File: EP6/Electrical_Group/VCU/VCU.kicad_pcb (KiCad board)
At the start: 4 copper layers, 150 x 120 mm, 328 parts, among them IC1 LMR50410Y3FQDBVRQ1, J1 MSD-4-A, J10 3V3out, J11 UPS_cap, J12 USBC_RPI_5Vonly, J13 USBA_RPI_5Vonly, J14 Rpi, J15 Dashboard, J16 STDC14, J17 CAN2, J18 CAN2_termination, J19 buzzer, J2 Conn_01x06, J20 I2C, J21 brakelight, J24 USB_C_stm32, J25 connector board, J3 I2C2, J4 NRST, J5 USART6, J6 DEBUG, J7 LVBattery, J8 24V_raw, J9 5Vout, Q1 AO3400A, Q2 2N7002, Q3 2N7002, SW1 VBUS, SW2 VBUS, U1 USB3300-EZK, U11 TCAN1042VDRQ1, U12 LSM6DSOX, U14 LM66100DCK, U15 USBLC6-2SC6, U2 STM32H743ZITx, U4 TPS5430DDA, U5 TPS5430DDA, U6 INA180A3, U7 INA180A3, U8 AMS1117-3.3, U9 LM66100DCK, Y1 8MHz X49SM8MSD2SC, Y2 32.768kHz Q13FC13500004, Y3 X322524MSB4SI

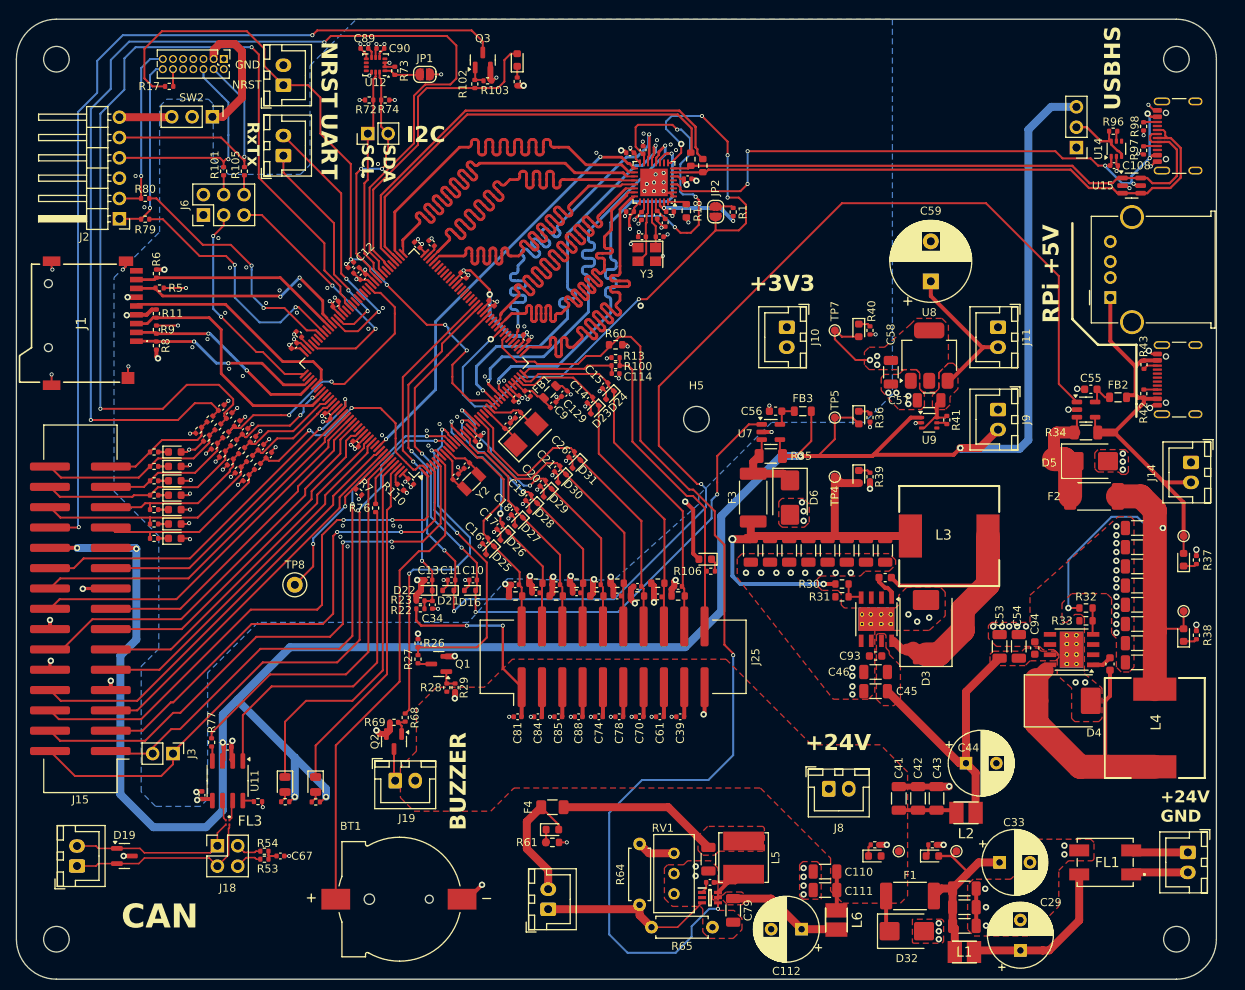
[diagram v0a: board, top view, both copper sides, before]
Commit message: add silkscreen on VCU PCB
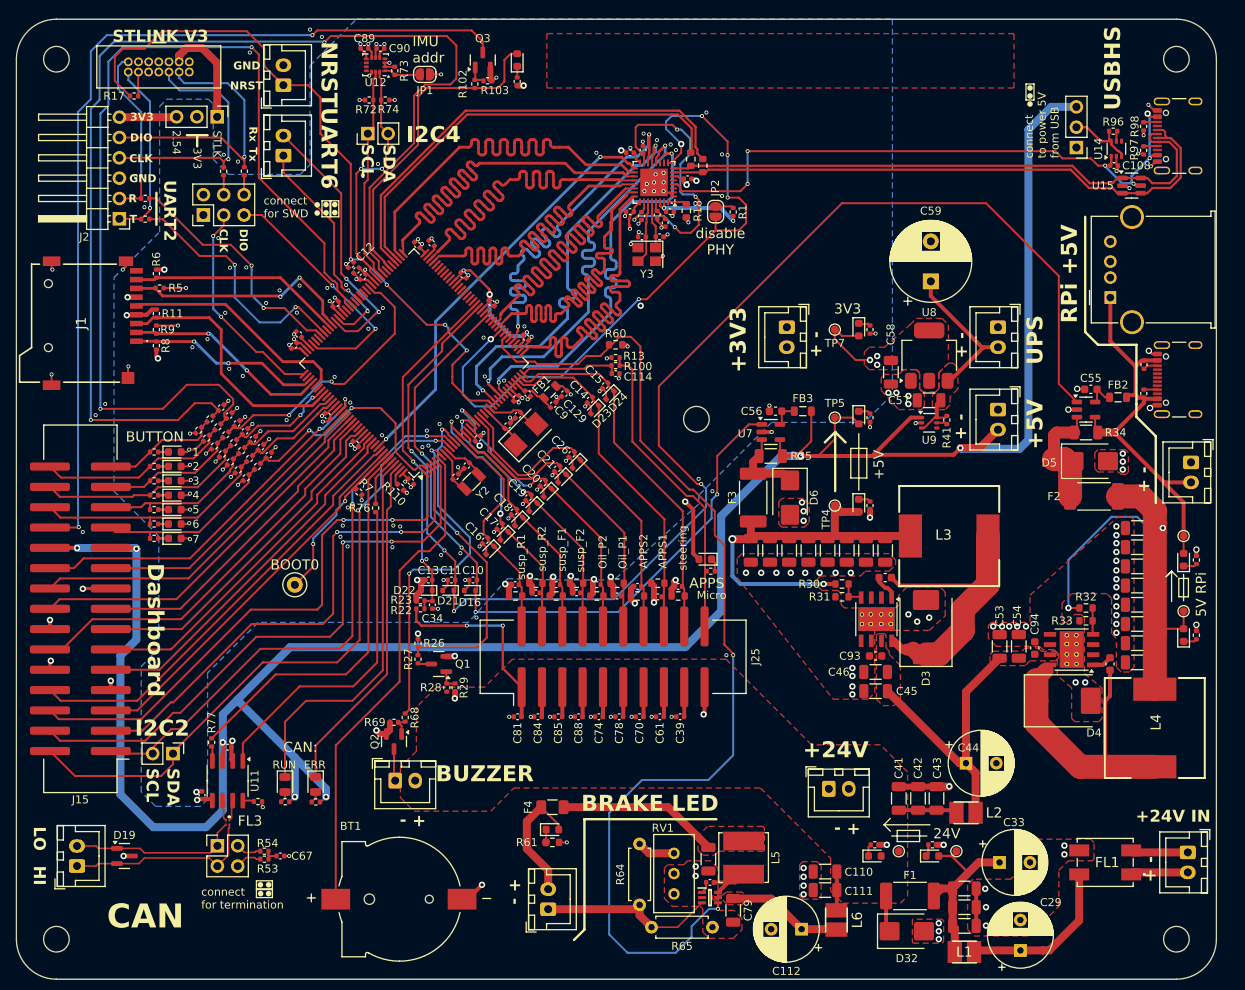
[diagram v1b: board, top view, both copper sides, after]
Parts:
- J16: footprint Connector_PinHeader_1.27mm:PinHeader_2x07_P1.27mm_Vertical -> nturt_kicad_lib_EP6:box_header_14P_pitch127
- moved R17 4.55 mm to (94.7, 49.6)
- moved J16 4.33 mm to (101.6, 45.3), turned to 0 degrees
- moved D10 3.60 mm to (185.3, 100.8)
- moved R39 3.60 mm to (186.7, 100.8)
- moved TP4 3.60 mm to (182.3, 100.8)
- moved SW2 0.60 mm to (105.1, 52.2)
- moved D11 0.10 mm to (185.3, 78.8)
- moved R40 0.10 mm to (186.7, 78.8)
- moved TP7 0.10 mm to (182.3, 78.8)
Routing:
- net /stlink & USB/t_DIO: track 30.6 -> 35.2 mm
- net /stlink & USB/t_CLK: track 27.2 -> 31.3 mm
- net /5V_3V3/5V_buck: track 53.3 -> 49.7 mm
- net /NRST: track 87.2 -> 90.3 mm
- net /stlink & USB/3V3_stlinkv3: track 15.9 -> 13.4 mm
- net Net-(U11-TXD): track 44.0 -> 42.0 mm
- net /RTDlight: track 114.7 -> 115.8 mm
- net /button7: track 144.8 -> 145.9 mm
- net /button6: track 121.6 -> 122.7 mm
- net /stlink & USB/t_NRST: track 2.19 -> 3.02 mm
- net GND: track 177.4 -> 177.3 mm, vias 224 -> 249
- added copper zone on F.Cu, net (none)
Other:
- board text added: "+ -"
- board text added: "+24V IN"
- board text added: "+5V"
- board text added: "1"
- board text added: "2"
- board text added: "2.54"
- board text added: "24V"
- board text added: "3"
- board text added: "3V3"
- board text added: "4"
- board text added: "5"
- board text added: "5V RPi"
- board text added: "6"
- board text added: "7"
- board text added: "APPS"
- board text added: "APPS1"
- board text added: "APPS2"
- board text added: "BOOT0"
- board text added: "BRAKE LED"
- board text added: "BUTTON"
- board text added: "CAN:"
- board text added: "CLK"
- board text added: "DIO"
- board text added: "Dashboard"
- board text added: "EP6 VCU RevA"
- board text added: "ERR"
- board text added: "HI"
- board text added: "I2C2"
- board text added: "I2C4"
- board text added: "IMU addr"
- board text added: "LO"
- board text added: "Micro"
- board text added: "Oil_P1"
- board text added: "Oil_P2"
- board text added: "R"
- board text added: "RUN"
- board text added: "STLINK V3"
- board text added: "STLK"
- board text added: "T"
- board text added: "UART2"
- board text added: "UART6"
- board text added: "UPS"
- board text added: "connect for SWD"
- board text added: "connect for termination"
- board text added: "connect to power 5V from USB"
- board text added: "disable PHY"
- board text added: "steering"
- board text added: "susp_F1"
- board text added: "susp_F2"
- board text added: "susp_R1"
- board text added: "susp_R2"
- board text removed: "+24V GND"
- board text removed: "I2C"
- board text removed: "UART"

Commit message: VCU snapshot
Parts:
- removed J2: Conn_01x06, Connector_PinHeader_2.54mm:PinHeader_1x06_P2.54mm_Horizontal
- removed SW2: VBUS, Connector_PinHeader_2.54mm:PinHeader_1x03_P2.54mm_Vertical
- added R2: 100R, Resistor_SMD:R_0402_1005Metric, F.Cu at (86.5, 51.0)
- TP8: footprint TestPoint:TestPoint_Loop_D2.50mm_Drill1.0mm -> TestPoint:TestPoint_Pad_D1.0mm
- moved C27 117.1 mm to (261.1, 10.7)
- moved TP3 116.4 mm to (279.2, 10.5)
- moved C28 111.8 mm to (261.1, 14.0)
- moved C37 106.4 mm to (261.1, 17.4)
- moved TP6 105.5 mm to (279.2, 13.6)
- moved C38 101.1 mm to (261.1, 20.7)
- moved L4 98.1 mm to (280.4, 49.6)
- moved R32 97.1 mm to (265.9, 31.8)
- moved R33 96.3 mm to (265.9, 34.3)
- moved C47 95.9 mm to (273.4, 43.2)
- moved C40 95.9 mm to (261.1, 24.1)
- moved U5 94.7 mm to (269.8, 43.8), turned to -90 degrees
- moved C94 94.0 mm to (269.8, 48.4), turned to 0 degrees
- moved D4 93.0 mm to (269.0, 52.6), turned to 180 degrees
- moved C48 90.8 mm to (261.1, 27.4)
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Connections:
- J16 pad 11: unconnected-(J16-Pin_11-Pad11) -> Net-(J16-Pin_11)
- J16 pad 3: /stlink & USB/3V3_stlinkv3 -> +3V3
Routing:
- net /5V_3V3/5V_buck_rpi: track 55.4 -> 18.2 mm, vias 2 -> 0
- net /5V_3V3/5V_buck_rpi_sw: track 36.6 -> 15.2 mm
- net /stlink & USB/t_DIO: track 35.2 -> 18.5 mm
- net +3V3: track 120.4 -> 134.4 mm
- net /stlink & USB/3V3_stlinkv3: track 13.4 -> 0.00 mm
- net /stlink & USB/t_CLK: track 31.3 -> 18.1 mm
- net +5V: track 307.4 -> 294.5 mm
- net /5V_3V3/Rpi_Vbus: track 52.7 -> 59.4 mm
- net /stlink & USB/3V3_dupont: track 6.57 -> 0.00 mm
- net /5V_3V3/24V_5VbuckIn: track 35.1 -> 29.2 mm
- net /SPI4_SCK: track 68.8 -> 65.1 mm
- net /5V_3V3/5V_buck_rpi_FB: track 3.33 -> 0.00 mm
- net /stlink & USB/VBUS: track 79.5 -> 82.3 mm
- net /stlink & USB/USART2_RX: track 22.0 -> 19.2 mm
- net /stlink & USB/USART2_TX: track 22.7 -> 20.1 mm
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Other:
- board text removed: "+24V IN"
- board text removed: "R"
- board text removed: "T"
- board text removed: "UART2"

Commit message: VCU snapshot
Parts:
- removed J6: DEBUG, Connector_PinHeader_2.54mm:PinHeader_2x03_P2.54mm_Vertical
- removed TP1: 24V_prefuse, TestPoint:TestPoint_Pad_D1.0mm
- added C52: 0u1, Capacitor_SMD:C_0402_1005Metric, F.Cu at (275.3, 152.1)
- added C62: 0u1, Capacitor_SMD:C_0402_1005Metric, F.Cu at (275.3, 154.1)
- added U3: SN74LVC4245APWR, Package_SO:TSSOP-24_4.4x7.8mm_P0.65mm, F.Cu at (269.5, 155.8)
- R18, R52, R99: footprint Resistor_SMD:R_0603_1608Metric -> Resistor_SMD:R_0402_1005Metric
- moved C112 160.1 mm to (138.2, 308.8)
- moved C76 160.1 mm to (126.6, 300.1)
- moved F4 160.1 mm to (107.1, 293.6)
- moved J21 160.1 mm to (106.5, 306.3)
- moved R65 160.1 mm to (127.1, 308.6)
- moved RV1 160.1 mm to (122.3, 299.3)
- moved C110 160.1 mm to (141.1, 301.6)
- moved C111 160.1 mm to (141.1, 303.9)
- moved C73 160.1 mm to (126.8, 303.0)
- moved C79 160.1 mm to (129.7, 306.5)
- moved L6 160.1 mm to (142.6, 307.7)
- moved R61 160.1 mm to (107.1, 298.0)
- moved R64 160.1 mm to (118.0, 298.1)
- moved D17 160.1 mm to (107.1, 296.4)
- moved IC1 160.1 mm to (126.8, 304.9)
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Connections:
- U2 pad 105: /SWDIO -> /T_DIO
- U2 pad 109: /SWCLK -> /T_CLK
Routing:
- net +5V: track 294.5 -> 0.00 mm, vias 8 -> 0
- net /I_measure_5vrpi: track 178.8 -> 0.00 mm, vias 4 -> 0
- net GND: track 178.6 -> 10.7 mm, vias 230 -> 0
- net /button7: track 145.9 -> 2.56 mm, vias 2 -> 0
- net /brake_gate: track 130.0 -> 0.00 mm, vias 2 -> 0
- net /button6: track 122.6 -> 2.56 mm, vias 2 -> 0
- net /RTDlight: track 115.8 -> 0.00 mm, vias 2 -> 0
- net +3V3: track 134.4 -> 28.2 mm, vias 50 -> 6
- net /I_measure_5v: track 93.7 -> 0.00 mm, vias 4 -> 0
- net /NRST: track 90.6 -> 0.00 mm, vias 4 -> 0
- net /PHY_RST: track 85.6 -> 0.00 mm, vias 6 -> 0
- net /stlink & USB/VBUS: track 82.3 -> 0.00 mm, vias 6 -> 0
- net /I2C2_SDA: track 81.3 -> 0.00 mm, vias 2 -> 0
- net /stlink & USB/USB_DP: track 74.9 -> 0.00 mm
- net /SPI4_MOSI: track 74.6 -> 0.00 mm, vias 2 -> 0
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- removed copper zone on F.Cu, net +24V
- removed copper zone on B.Cu, net +3V3
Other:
- outline, holes or cut-outs redrawn
- board text removed: "CLK"
- board text removed: "DIO"
- board text removed: "RPi +5V"
- board text removed: "STLINK V3"
- board text removed: "disable PHY"

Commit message: VCU initial layout
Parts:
- removed J3: I2C2, Connector_PinHeader_2.54mm:PinHeader_1x02_P2.54mm_Vertical
- removed R52, R99: 0, Resistor_SMD:R_0402_1005Metric
- removed SW1: VBUS, Connector_PinHeader_2.54mm:PinHeader_1x03_P2.54mm_Vertical
- added J6: USB_SEL, Connector_PinHeader_2.54mm:PinHeader_2x03_P2.54mm_Vertical_SMD, F.Cu at (121.2, 54.8)
- added R10: 0R, Resistor_SMD:R_0603_1608Metric_Pad0.98x0.95mm_HandSolder, F.Cu at (101.3, 108.2)
- added R12: 0R, Resistor_SMD:R_0603_1608Metric_Pad0.98x0.95mm_HandSolder, F.Cu at (101.3, 109.8)
- added R14: 0R, Resistor_SMD:R_0603_1608Metric_Pad0.98x0.95mm_HandSolder, F.Cu at (101.3, 111.4)
- added R3: 0R, Resistor_SMD:R_0603_1608Metric_Pad0.98x0.95mm_HandSolder, F.Cu at (101.3, 105.0)
- added R4: 0R, Resistor_SMD:R_0603_1608Metric_Pad0.98x0.95mm_HandSolder, F.Cu at (101.3, 106.6)
- J12: moved to B.Cu
- R60: footprint Resistor_SMD:R_0603_1608Metric -> Resistor_SMD:R_0402_1005Metric
- moved TP7 226.2 mm to (91.8, 158.4)
- moved R65 216.2 mm to (170.8, 96.8), turned to -90 degrees
- moved J21 210.3 mm to (176.3, 108.0), turned to -90 degrees
- moved RV1 209.8 mm to (164.4, 93.8), turned to -135 degrees
- moved D11 209.6 mm to (84.4, 128.2), turned to 180 degrees
- moved R40 208.7 mm to (87.0, 128.2), turned to 0 degrees
- moved R64 207.4 mm to (167.6, 96.8)
- moved J9 204.9 mm to (91.9, 121.3)
- moved J11 204.8 mm to (101.8, 121.3)
- moved C59 200.6 mm to (108.2, 123.4), turned to 0 degrees
- moved R41 199.9 mm to (98.4, 129.0), turned to 90 degrees
- moved C112 199.0 mm to (168.0, 112.0), turned to 90 degrees
- moved J10 198.4 mm to (84.7, 121.3)
- moved C79 196.4 mm to (159.8, 112.4), turned to 90 degrees
- moved U9 196.3 mm to (100.6, 128.6), turned to 180 degrees
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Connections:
- J15 pad 3: /SPI4_CS -> /SPI4_CS_5VTTL
- J15 pad 4: /SPI4_MOSI -> /SPI4_MOSI_5VTTL
- J15 pad 5: /SPI4_LEDPWM -> /SPI4_LEDPWM_5VTTL
- J15 pad 6: /SPI4_SCK -> /SPI4_SCK_5VTTL
- R96 pad 1: Net-(SW1-B) -> +5V
- U1 pad 7: /stlink & USB/USB_DP -> /stlink & USB/HSPHY_D_P
- U1 pad 8: /stlink & USB/USB_DN -> /stlink & USB/HSPHY_D_N
- U14 pad 3: Net-(SW1-B) -> +5V
- U14 pad 6: Net-(SW1-B) -> +5V
- U2 pad 103: unconnected-(U2-PA11-Pad103) -> /USBFS_D_N
- U2 pad 104: unconnected-(U2-PA12-Pad104) -> /USBFS_D_P
- U2 pad 34: /APPS2 -> /APPSmicro
- U2 pad 35: /steering -> /APPS2
- U2 pad 36: /APPSmicro -> /steering
- U2 pad 75: /D_N -> /USBHS_D_N
- U2 pad 76: /D_P -> /USBHS_D_P
- U3 pad 10: /DISP_CS -> /SPI4_LEDPWM_5VTTL
- U3 pad 14: /SPI2_CS -> /SPI4_LEDPWM
- U3 pad 15: /SPI2_SCK -> GND
- U3 pad 16: /SPI2_MOSI -> GND
- U3 pad 17: GND -> /SPI4_MOSI
- U3 pad 18: GND -> /SPI4_MISO
- U3 pad 19: GND -> /SPI4_CS
- U3 pad 20: GND -> /SPI4_SCK
- U3 pad 4: unconnected-(U3-A2-Pad4) -> /SPI4_SCK_5VTTL
- U3 pad 5: unconnected-(U3-A3-Pad5) -> /SPI4_CS_5VTTL
- U3 pad 6: unconnected-(U3-A4-Pad6) -> /SPI4_MISO_5VTTL
- U3 pad 7: unconnected-(U3-A5-Pad7) -> /SPI4_MOSI_5VTTL
- U3 pad 8: /DISP_DIN -> unconnected-(U3-A6-Pad8)
- U3 pad 9: /DISP_CLK -> unconnected-(U3-A7-Pad9)
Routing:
- net GND: track 10.7 -> 233.4 mm, vias 0 -> 44
- net +3V3: track 28.2 -> 241.2 mm, vias 6 -> 11
- net +5V: track 0.00 -> 127.6 mm, vias 0 -> 5
- net +24V: track 0.00 -> 119.8 mm
- net /24V_measureV: track 0.00 -> 110.6 mm, vias 0 -> 2
- net /VBAT: track 0.00 -> 95.0 mm, vias 0 -> 2
- net /NRST: track 0.00 -> 92.1 mm, vias 0 -> 4
- net /I_measure_5v: track 0.00 -> 82.5 mm, vias 0 -> 3
- net /brake_gate: track 0.00 -> 63.1 mm, vias 0 -> 5
- net /I2C2_SDA: track 0.00 -> 59.4 mm, vias 0 -> 2
- net /I2C2_SCL: track 0.00 -> 55.8 mm, vias 0 -> 2
- net /5V_3V3/5V_buck_rpi: track 0.00 -> 49.3 mm
- net /electrical1/CAN2_H: track 0.00 -> 47.0 mm, vias 0 -> 1
- net /24V_lowTrig: track 0.00 -> 44.9 mm, vias 0 -> 2
- net /USBHS.DATA1: track 0.00 -> 44.2 mm
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- removed copper zone on F.Cu, net +3V3
- removed copper zone on F.Cu, net /5V_3V3/24V_5VbuckIn
- removed copper zone on F.Cu, net /5V_3V3/5V_proUPS
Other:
- board size 150 x 120 mm -> 100 x 100 mm
- board text removed: "2.54"
- board text removed: "BRAKE LED"
- board text removed: "EP6 VCU RevA"
- board text removed: "HI"
- board text removed: "LO"
- board text removed: "STLK"
- board text removed: "connect to power 5V from USB"
